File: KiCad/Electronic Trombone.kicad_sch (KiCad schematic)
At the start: 3 parts, among them J1 691137710002

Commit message: amplifier sch., general changes to oscillator sch.
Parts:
- removed J1: 691137710002, Header 691137710002:691137710002, symbol 691137710002:691137710002
- added J1: 691137710003, 691137710003:691137710003, symbol Header 691137710003:691137710003
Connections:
- net +12V renamed +9V
- net -12V renamed -9V
- new net V_in: J1.1
- new net V_out: J1.2
- new net V_trigger: J1.3
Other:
- removed sheet Power Supply
- added sheet Amplifier (Amplifier.kicad_sch)
- added sheet Filter (Filter.kicad_sch)
- sheet Envelope Generator ports: added Amplifier Out, Filter Out; removed Out
- note added: "0V to -2V"
- note added: "10mV pp."
- note added: "Centered at 0V"
- moved on the sheet: B1, B2

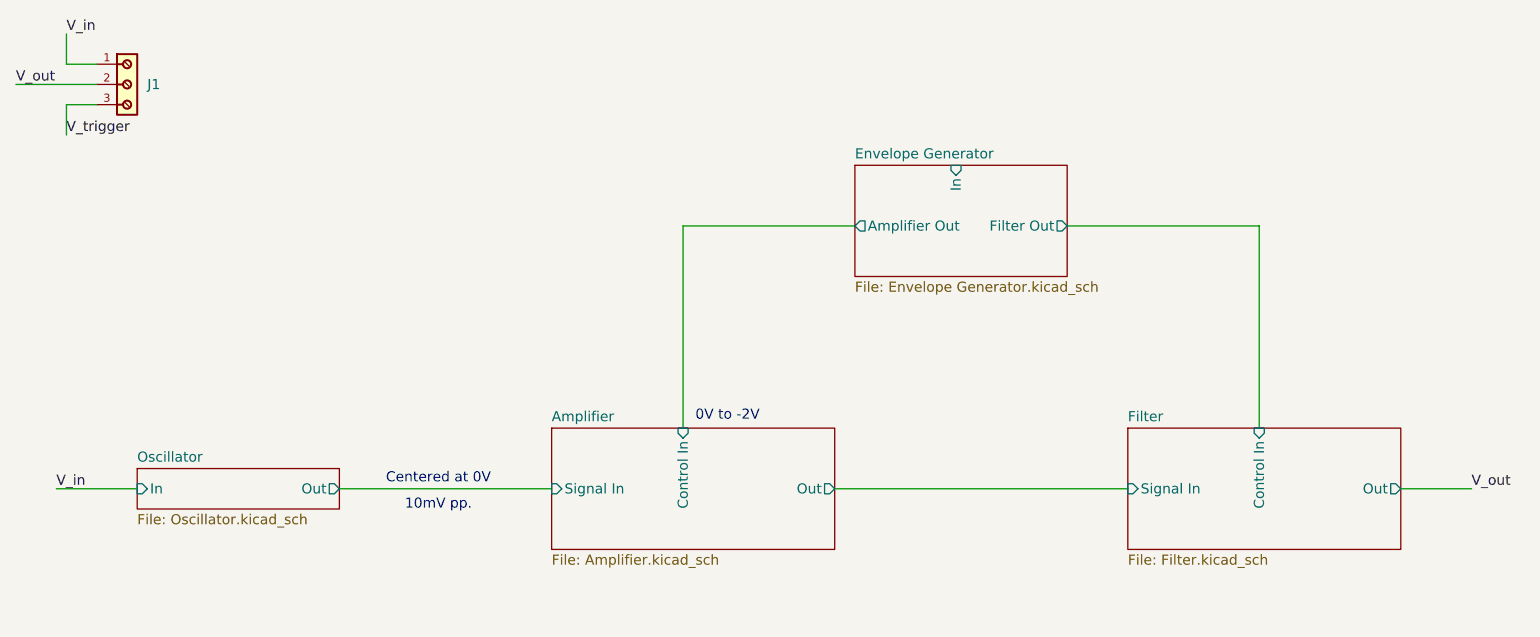
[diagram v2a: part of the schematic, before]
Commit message: improved osc.'s output buffer cct., swap filter & amp
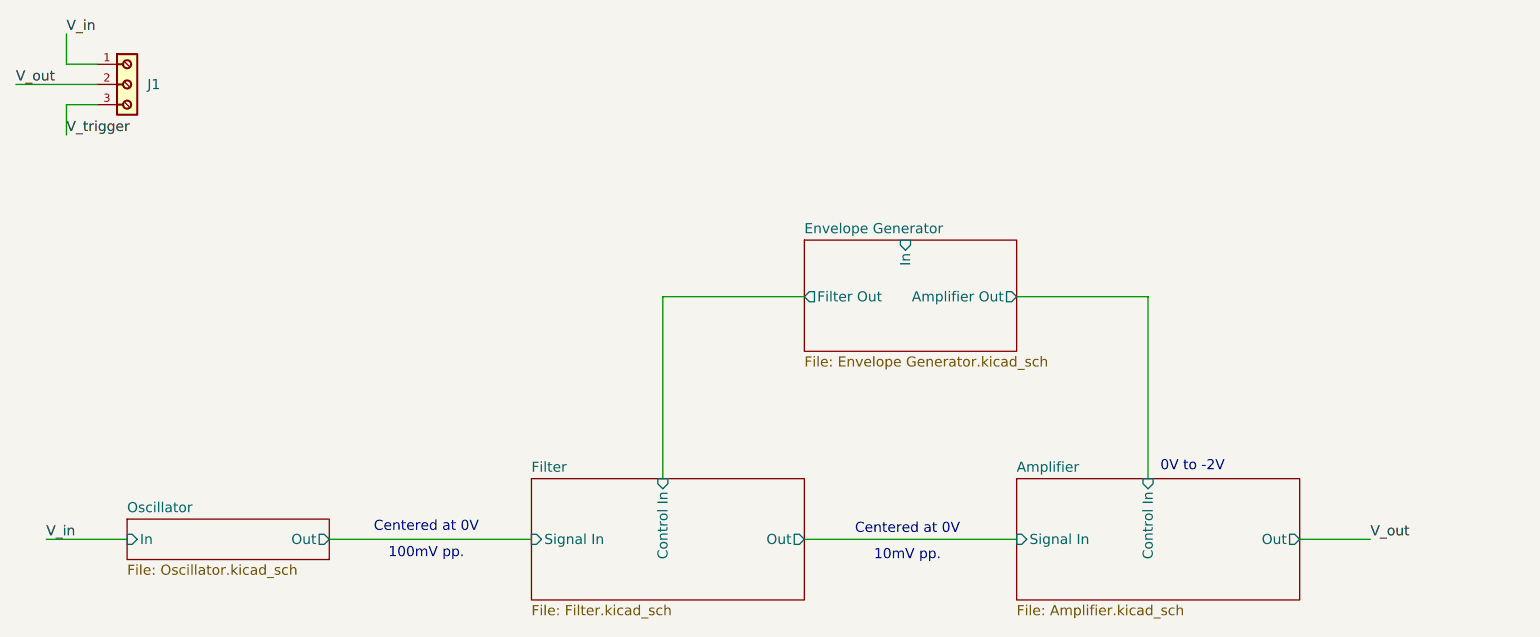
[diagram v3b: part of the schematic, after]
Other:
- note added: "100mV pp."

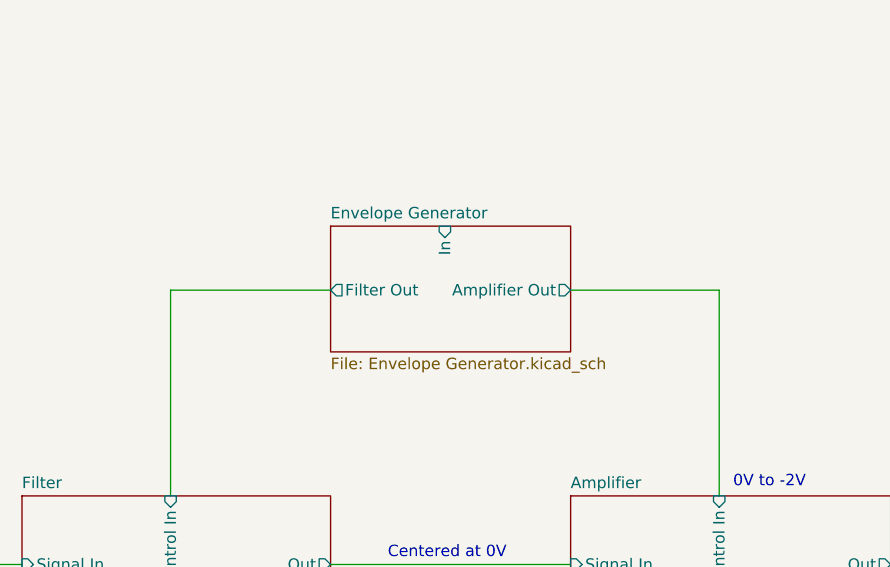
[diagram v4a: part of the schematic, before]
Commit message: drafted a dual output envelope generator
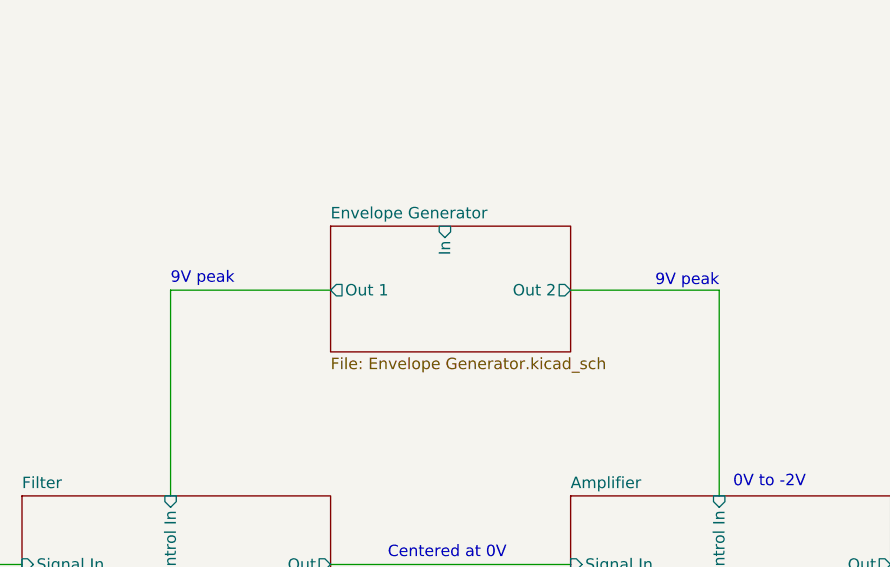
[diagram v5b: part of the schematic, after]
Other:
- sheet Envelope Generator ports: added Out 1, Out 2; removed Amplifier Out, Filter Out
- note added: "9V peak"
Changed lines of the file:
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@@
+		)
+	)
+	(text "9V peak"
+		(exclude_from_sim no)
+		(at 105.156 86.36 0)
+		(effects
+			(font
+				(size 1.27 1.27)
+			)
 		)
 	)
@@
 		(exclude_from_sim no)
 		(at 71.882 119.888 0)
+		(effects
+			(font
+				(size 1.27 1.27)
+			)
+		)
+	)
+	(text "9V peak"
+		(exclude_from_sim no)
+		(at 159.004 86.614 0)
 		(effects
 			(font
@@
 			)
 		)
-		(pin "Amplifier Out" output
+		(pin "Out 1" output
+			(at 119.38 87.63 180)
+			(effects
+				(font
+					(size 1.27 1.27)
+				)
+				(justify left)
+			)
+		)
+		(pin "Out 2" output
 			(at 146.05 87.63 0)
 			(effects
@@
 			)
 		)
-		(pin "Filter Out" output
-			(at 119.38 87.63 180)
-			(effects
-				(font
-					(size 1.27 1.27)
-				)
-				(justify left)
-			)
-		)

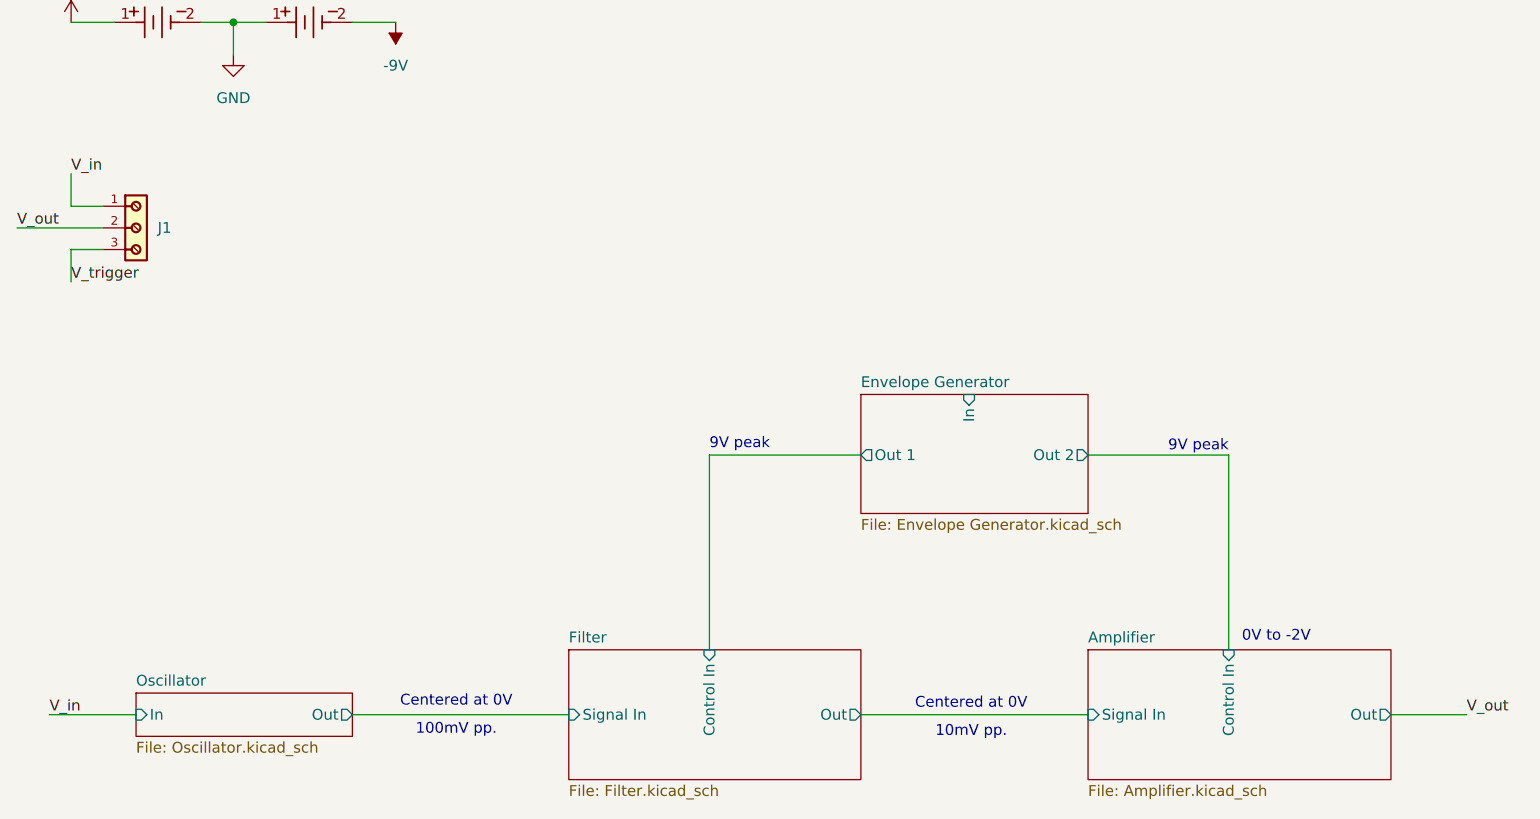
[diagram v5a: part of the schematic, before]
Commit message: wrote ac analysis for filter, stepping through CVs
I was trying to find the relationship between the filter's cutoff frequency and the its control voltage. As it turns out, the relationship is exponential (i.e. a linear increase in CV results in an exponential increase in cutoff freq).
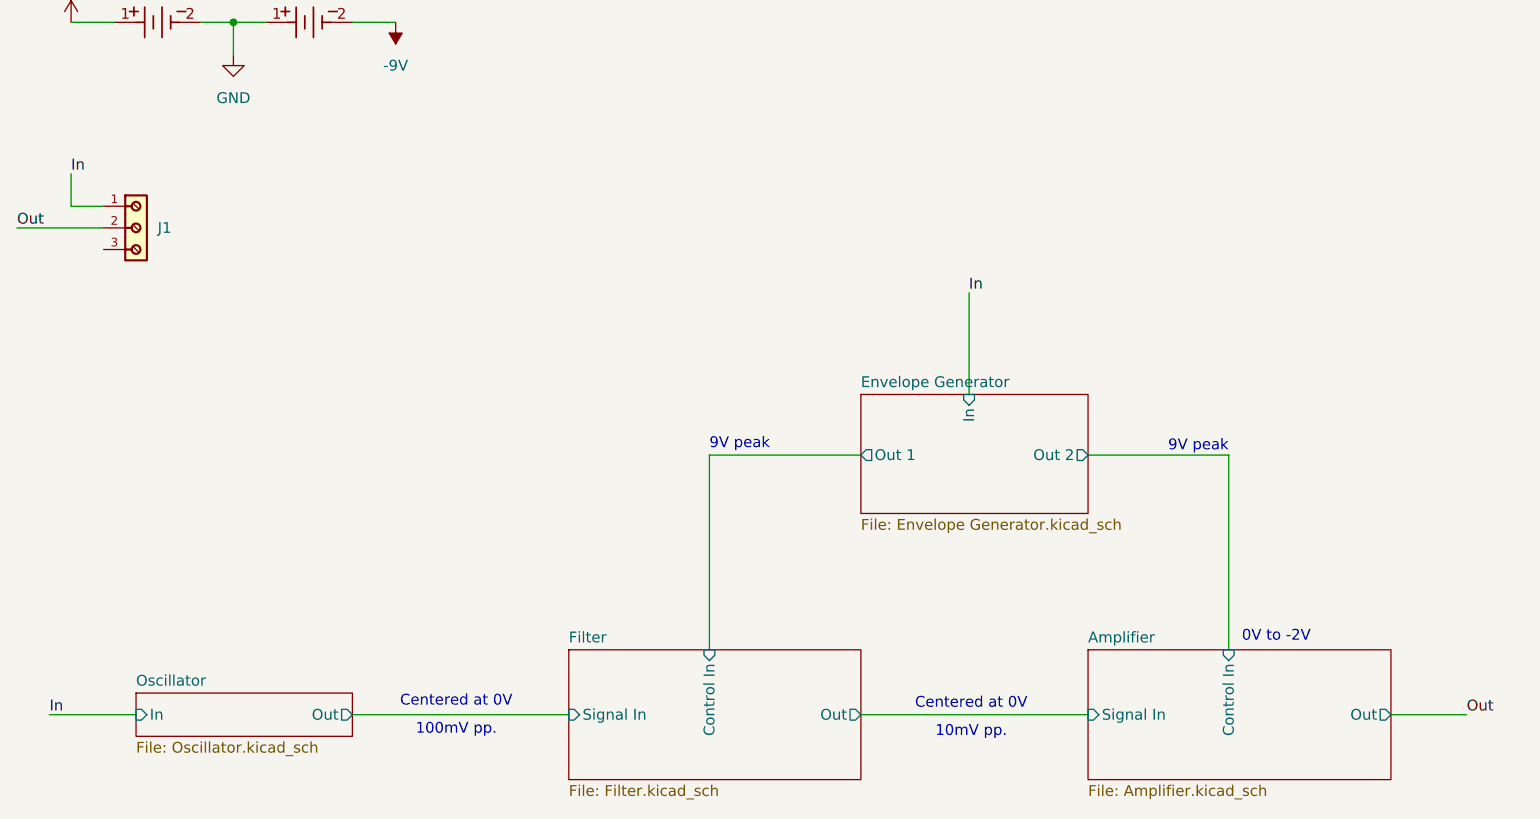
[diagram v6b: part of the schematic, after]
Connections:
- net V_in renamed In
- net V_out renamed Out
- net V_trigger: no longer names the net of J1.3
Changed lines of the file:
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@@
 	(wire
 		(pts
-			(xy 30.48 63.5) (xy 26.67 63.5)
+			(xy 132.08 68.58) (xy 132.08 80.518)
 		)
 		(stroke
@@
 	(wire
 		(pts
-			(xy 26.67 63.5) (xy 26.67 67.31)
+			(xy 45.72 36.83) (xy 49.53 36.83)
 		)
 		(stroke
@@
 		)
 	)
-	(wire
-		(pts
-			(xy 45.72 36.83) (xy 49.53 36.83)
-		)
-		(stroke
-			(width 0)
-			(type default)
-		)
-	)
-	(label "V_trigger"
-		(at 26.67 67.31 0)
+	(label "In"
+		(at 132.08 68.58 0)
 		(effects
 			(font
@@
 		)
 	)
-	(label "V_in"
+	(label "In"
 		(at 24.13 118.11 0)
 		(effects
@@
 		)
 	)
-	(label "V_in"
+	(label "In"
 		(at 26.67 54.61 0)
 		(effects
@@
 		)
 	)
-	(label "V_out"
+	(label "Out"
 		(at 20.32 60.96 0)
 		(effects
@@
 		)
 	)
-	(label "V_out"
+	(label "Out"
 		(at 190.5 118.11 0)
 		(effects
@@
 		(on_board yes)
 		(dnp no)
-		(fields_autoplaced yes)
 		(stroke
 			(width 0.1524)

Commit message: finalizing schematic
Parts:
- removed J1: 691137710003, 691137710003:691137710003, symbol Header 691137710003:691137710003
- added J1: 691137710004, 691137710004:691137710004, symbol Header 691137710004:691137710004
- added R1, R2, R3, R5, R7, R8: R_US, symbol Device:R_US
- added R4, R6: 10k, symbol Device:R_US
- added U1, U3: TL074, symbol Amplifier_Operational:TL074
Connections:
- net GND: now also R2.1, U1.13 (-), U1.6 (-), U1.9 (-)
- net In: now also U1.1, U1.2 (-)
- net Out: now also J1.2, R1.2, U3.14
- new net: R4.1, R6.2, U1.12 (+)
- new net: R3.1, R5.2, U1.5 (+)
- new net: R3.2, R6.1, U1.7
- new net: R7.1, R8.2, U1.10 (+)
- new net: R1.1, R2.2, U3.13 (-)
- new net Amp Control: R7.2, U1.8
- new net Amplifier/Out: U3.12 (+)
- new net Envelope Generator/Out Amp: R8.1
- new net Envelope Generator/Out Filter: R5.1
- new net Filter Control: R4.2, U1.14
- new net Pot Negative: J1.4
- new net Pot Positive: J1.3
- new net Unprocessed In: J1.1, U1.3 (+)
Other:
- sheet Envelope Generator ports: added Out Amp, Out Filter; removed Out 1, Out 2
- note removed: "0V to -2V"
- note removed: "9V peak"
- moved on the sheet: B1, B2
